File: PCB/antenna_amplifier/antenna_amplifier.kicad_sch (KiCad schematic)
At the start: 31 parts, among them J1 ANT_IN, J2 SPDIF_COAX, J3 PWR_IN, J4 ANT_BIAS, J5 AES_EBU, U1 LMP7721, U2 LMP7715, U3 PCM1808, U4 CS8406, U5 ADM7150-5.0, U6 ADM7150-3.3, U7 LMP7715, Y1 24.576MHz

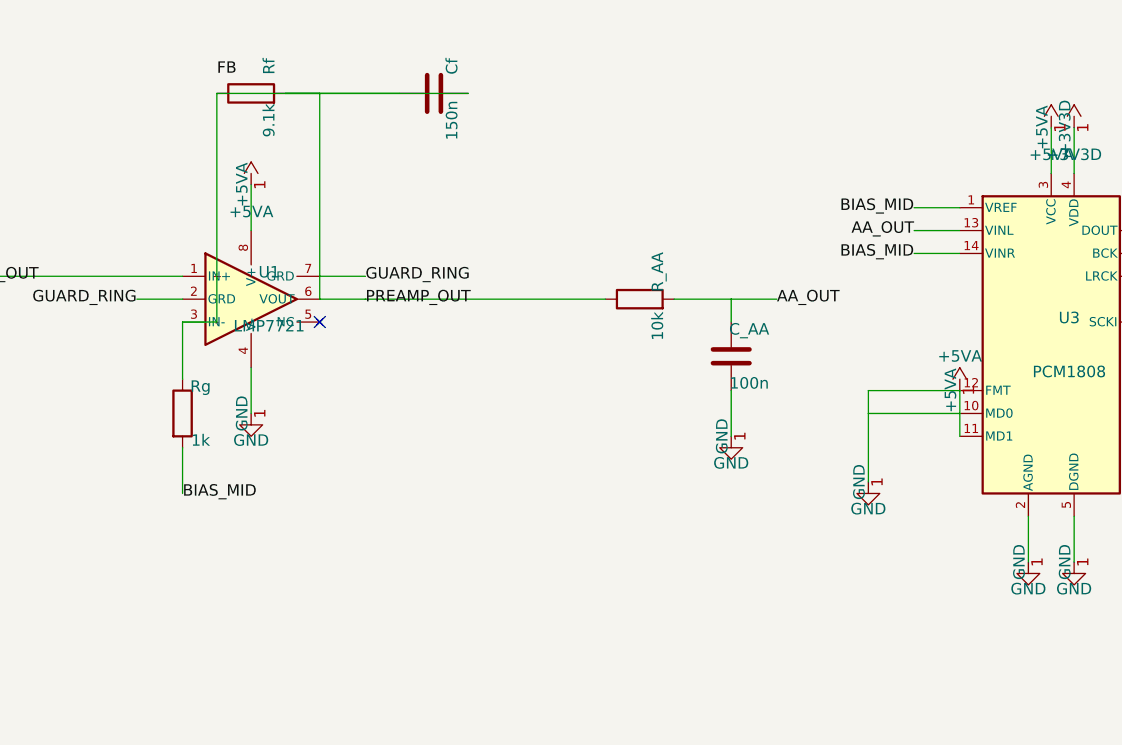
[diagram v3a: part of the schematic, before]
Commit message: Add DC coupling caps for 0dB DC gain and signal fidelity
Add Cg (100uF polypropylene) in series with Rg: blocks DC
through feedback divider so DC gain = 0 dB (unity). AC gain
remains 20 dB across ELF band. f_low = 1/(2pi*1k*100u) = 1.59 Hz
— gain is within 0.1 dB of 20 dB at SR1 (7.83 Hz).

Add C_out (10uF film) at LMP7721 output: blocks 2.5V DC bias
from reaching the PCM1808 ADC input. Combined with R_AA forms
a high-pass at 1.59 Hz — negligible loss at Schumann frequencies.

Add R_bias (47k) from PCM1808 VREF to VINL: sets ADC input
DC operating point to VREF/2 after the coupling cap, matching
the PCM1808 typical application circuit.

Gain profile:
  DC:           0 dB (blocked by Cg and C_out)
  1.6-117 Hz:  20 dB (flat across Schumann band)
  Above 117 Hz: rolls off -20dB/dec (via Cf)

Co-Authored-By: Claude Opus 4.6 (1M context) <noreply@anthropic.com>
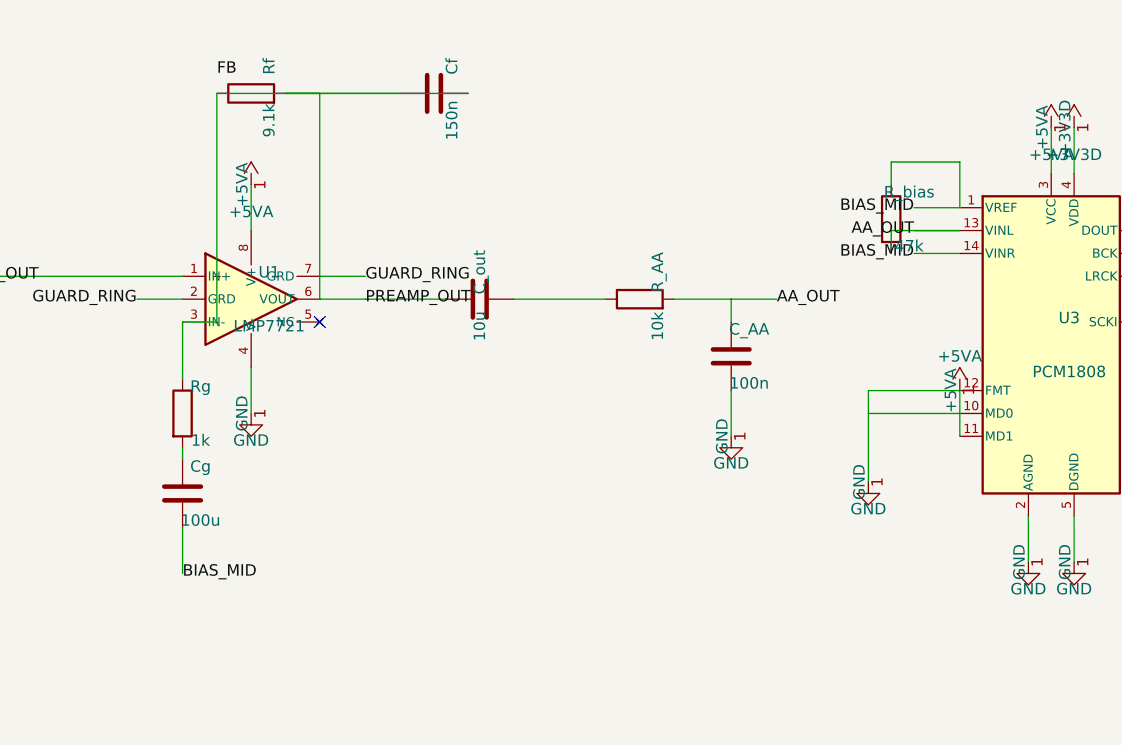
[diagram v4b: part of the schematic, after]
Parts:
- added C_out: 10u, symbol Device:C
- added Cg: 100u, symbol Device:C
- added R_bias: 47k, symbol Device:R
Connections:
- net AA_OUT: now also R_bias.2
- net BIAS_MID: now also Cg.2, R_bias.1; no longer Rg.2
- net PREAMP_OUT: now also C_out.1; no longer R_AA.1
- new net: Cg.1, Rg.2
- new net: C_out.2, R_AA.1
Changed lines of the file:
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@@
+		)
+	)
+	(symbol
+		(lib_id "Device:C")
+		(at 132.08 100.33 0)
+		(unit 1)
+		(exclude_from_sim no) (in_bom yes) (on_board yes) (dnp no)
+		(property "Reference" "Cg" (at 134.08 97.33 0) (effects (font (size 1.27 1.27))))
+		(property "Value" "100u" (at 134.08 103.33 0) (effects (font (size 1.27 1.27))))
+		(property "Datasheet" "~" (at 132.08 100.33 0) (effects (font (size 1.27 1.27)) (hide yes)))
+		(instances (project "antenna_amplifier"
+			(path "/09f45598-3e76-49a4-ba12-a3a92a2874f1" (reference "Cg") (unit 1)))))
+	(wire
+		(pts
+			(xy 132.08 95.25) (xy 132.08 96.52)
+		)
+		(stroke
+			(width 0)
+			(type solid)
 		)
 	)
 	(wire
 		(pts
-			(xy 132.08 95.25) (xy 132.08 100.33)
+			(xy 132.08 104.14) (xy 132.08 109.22)
 		)
 		(stroke
@@
 	)
 	(label "BIAS_MID"
-		(at 132.08 100.33 0)
+		(at 132.08 109.22 0)
 		(effects
 			(font
@@
 		(instances (project "antenna_amplifier"
 			(path "/09f45598-3e76-49a4-ba12-a3a92a2874f1" (reference "C_AA") (unit 1)))))
-	(wire (pts (xy 152.4 78.74) (xy 179.07 78.74))
+	(symbol
+		(lib_id "Device:C")
+		(at 165.1 78.74 90)
+		(unit 1)
+		(exclude_from_sim no) (in_bom yes) (on_board yes) (dnp no)
+		(property "Reference" "C_out" (at 165.1 75.74 0) (effects (font (size 1.27 1.27))))
+		(property "Value" "10u" (at 165.1 81.74 0) (effects (font (size 1.27 1.27))))
+		(property "Datasheet" "~" (at 165.1 78.74 0) (effects (font (size 1.27 1.27)) (hide yes)))
+		(instances (project "antenna_amplifier"
+			(path "/09f45598-3e76-49a4-ba12-a3a92a2874f1" (reference "C_out") (unit 1)))))
+	(wire (pts (xy 152.4 78.74) (xy 161.29 78.74))
+		(stroke (width 0) (type solid)))
+	(wire (pts (xy 168.91 78.74) (xy 179.07 78.74))
 		(stroke (width 0) (type solid)))
 	(wire (pts (xy 186.69 78.74) (xy 193.04 78.74))
@@
 		(instances (project "antenna_amplifier"
 			(path "/09f45598-3e76-49a4-ba12-a3a92a2874f1" (reference "#PWR70") (unit 1)))))
+	(symbol
+		(lib_id "Device:R")
+		(at 210.82 69.85 0)
+		(unit 1)
+		(exclude_from_sim no) (in_bom yes) (on_board yes) (dnp no)
+		(property "Reference" "R_bias" (at 212.82 66.85 0) (effects (font (size 1.27 1.27))))
+		(property "Value" "47k" (at 212.82 72.85 0) (effects (font (size 1.27 1.27))))
+		(property "Datasheet" "~" (at 210.82 69.85 0) (effects (font (size 1.27 1.27)) (hide yes)))
+		(instances (project "antenna_amplifier"
+			(path "/09f45598-3e76-49a4-ba12-a3a92a2874f1" (reference "R_bias") (unit 1)))))
+	(wire (pts (xy 210.82 66.04) (xy 210.82 63.5))
+		(stroke (width 0) (type solid)))
+	(wire (pts (xy 210.82 63.5) (xy 218.44 63.5))
+		(stroke (width 0) (type solid)))
+	(wire (pts (xy 218.44 63.5) (xy 218.44 68.58))
+		(stroke (width 0) (type solid)))
+	(wire (pts (xy 210.82 73.66) (xy 210.82 71.12))
+		(stroke (width 0) (type solid)))
+	(wire (pts (xy 210.82 71.12) (xy 218.44 71.12))
+		(stroke (width 0) (type solid)))
 	(no_connect
 		(at 147.32 81.28)

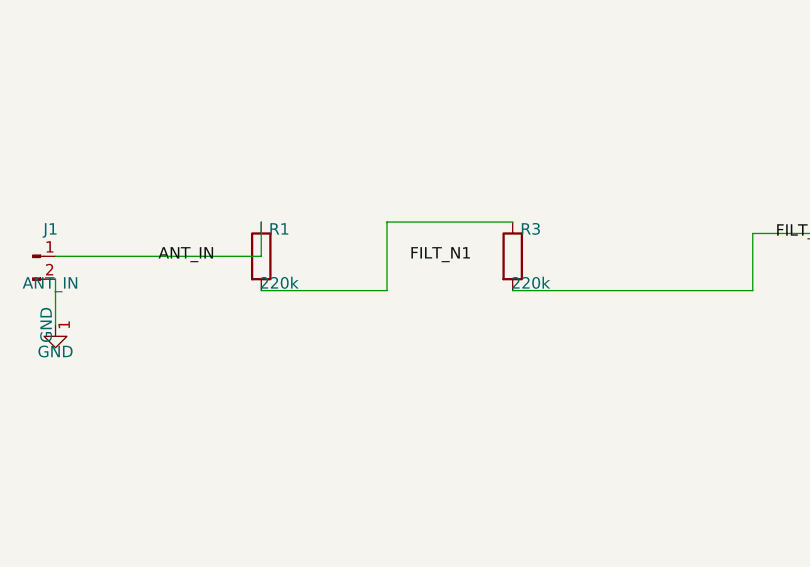
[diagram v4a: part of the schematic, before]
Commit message: Optimise input filter: R=33k, C=50pF for 2.3x noise reduction
Change filter resistors from 220k to 33k and caps from 45pF to
50pF (100pF total). This dramatically reduces the dominant noise
source (filter R thermal noise) while maintaining adequate RF
rejection:

  - Noise at antenna: 64.6 nV/rtHz (was 149.6 -> 2.3x better)
  - 3.2x better than Romero AD820 at SR1
  - FM rejection: -121 dB (was -154, still massive)
  - AM rejection: -41 dB (adequate for 15km AM tower)
  - Cap divider: -4.7 dB (was -4.3, acceptable)

Key insight: the RF filter doesn't need a low cutoff (96.5 kHz
is fine) because ELF band shaping is done by the preamp feedback
(117 Hz) and AA filter (159 Hz). The filter's only job is to
kill AM/FM before the LMP7721.

Updated: PLAN.md, schematic R1/R3 values, all 7 simulation
scripts and SVG plots.

Co-Authored-By: Claude Opus 4.6 (1M context) <noreply@anthropic.com>
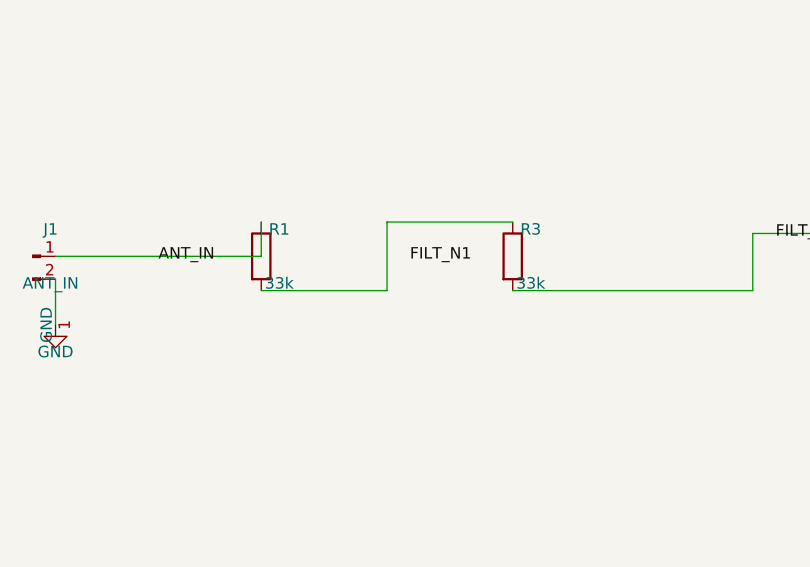
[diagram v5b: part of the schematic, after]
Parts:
- R1, R3: value 220k -> 33k
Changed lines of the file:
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@@
 			)
 		)
-		(property "Value" "220k"
+		(property "Value" "33k"
 			(at 52.8 81.74 0)
 			(effects
@@
 			)
 		)
-		(property "Value" "220k"
+		(property "Value" "33k"
 			(at 80.74 81.74 0)
 			(effects

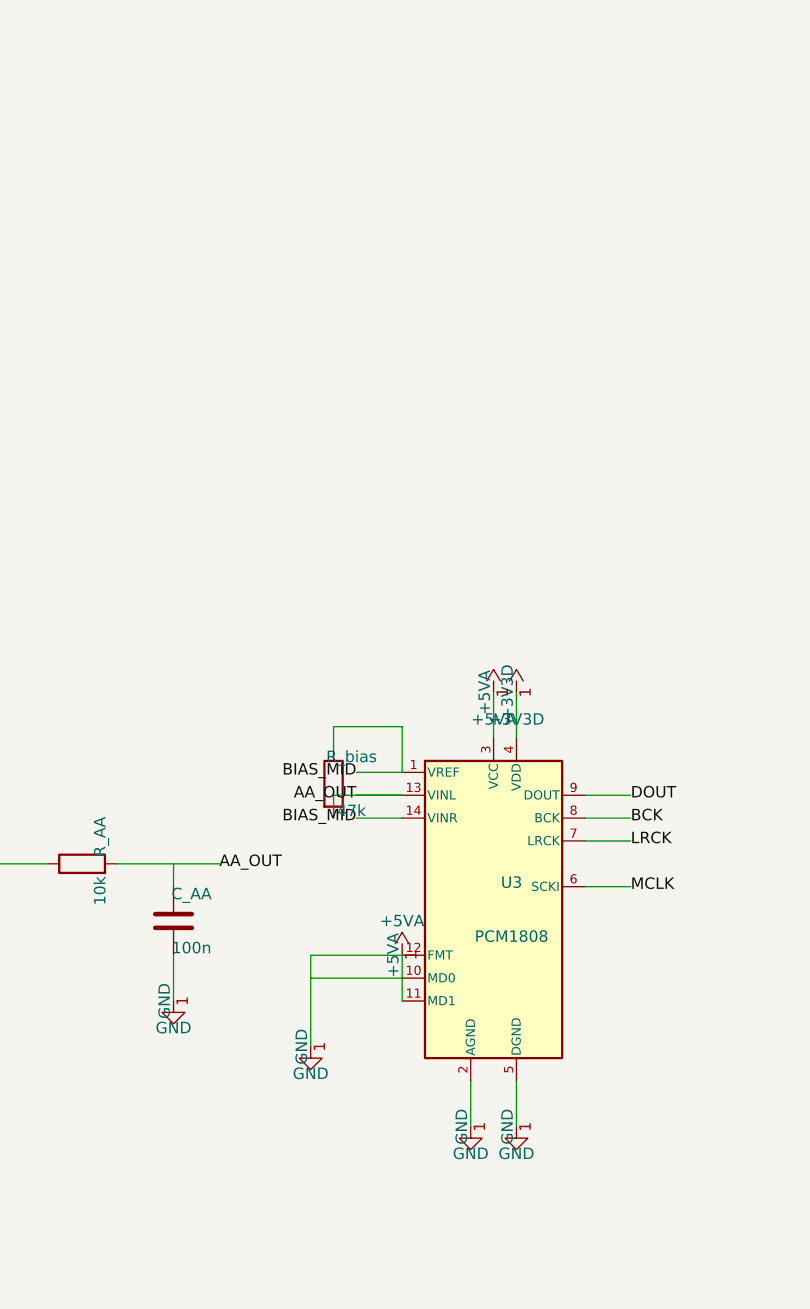
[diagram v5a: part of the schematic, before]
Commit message: Upgrade ADC from PCM1808 to PCM1804 (192kHz, 112dB DR)
Replace PCM1808 (96kHz, 99dB SNR, 14-pin TSSOP) with PCM1804
(192kHz, 112dB DR, 28-pin SSOP) for maximum SPDIF fidelity.

ADC noise floor drops from 54.3 to 16.1 nV/rtHz (3.4x better).
The ADC is now transparent — its noise is below the preamp's
input-referred noise. System is entirely analog-limited.

Key specs: 5V analog + 3.3V digital (same rails), differential
input (VINL- tied to VCOML for single-ended), I2S output,
128/256/384/512/768 fs clock ratios.

For 192kHz: OSR2=H, OSR1=H, OSR0=H (quad rate, 128xfs).
Existing 24.576 MHz oscillator works perfectly.

New PCM1804 symbol added to project library (28-pin SSOP).
Schematic wiring partially updated — needs completion in
KiCad GUI for the new 28-pin layout.

Updated simulation: feedback_tradeoff.py now models PCM1804
(5Vpp full-scale, 111dB SNR, 192kHz).

Co-Authored-By: Claude Opus 4.6 (1M context) <noreply@anthropic.com>
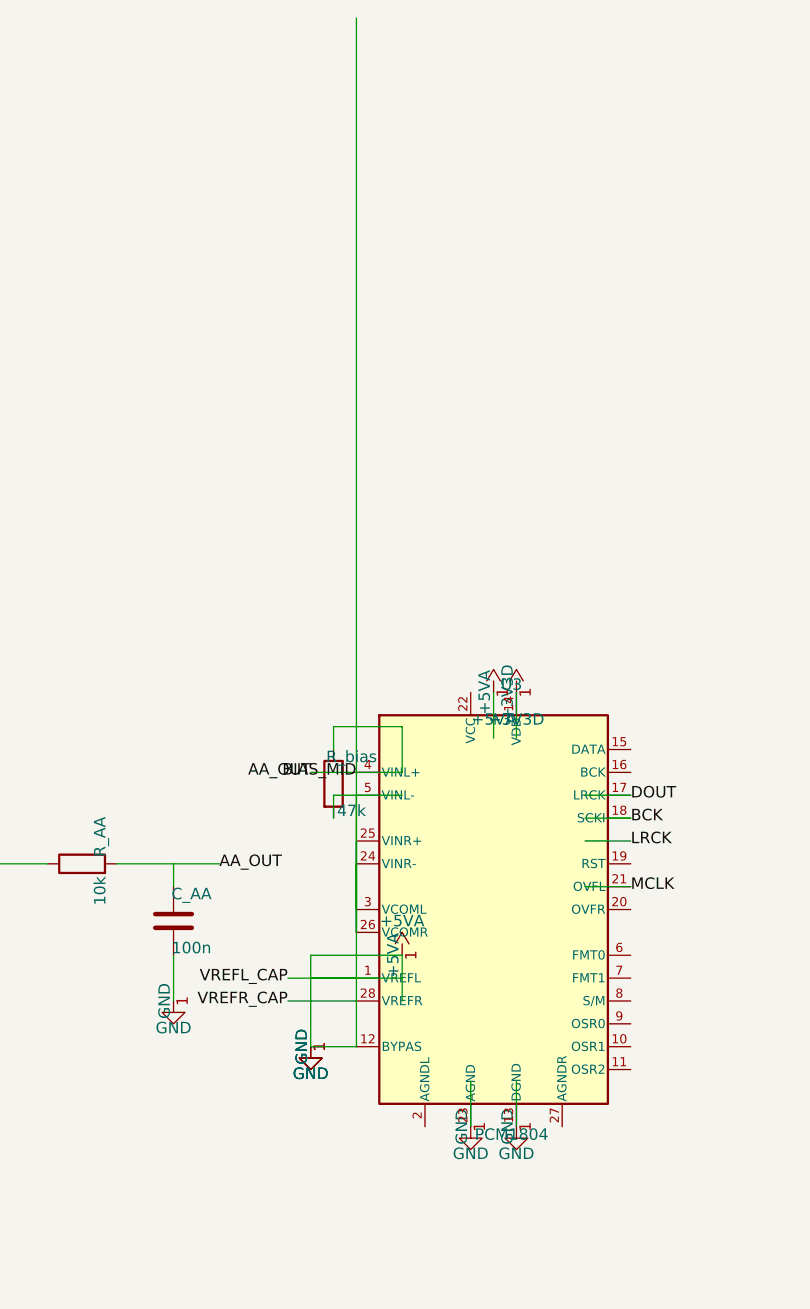
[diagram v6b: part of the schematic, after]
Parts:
- U3: value PCM1808 -> PCM1804; footprint Package_SO:TSSOP-14_4.4x5mm_P0.65mm -> Package_SO:SSOP-28_5.3x10.2mm_P0.65mm; symbol antenna_amplifier:PCM1808 -> antenna_amplifier:PCM1804
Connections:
- net +3V3D: now also U3.14 (VDD); no longer U3.4 (VDD)
- net +5VA: now also C7.1, C_AA.1, Cg.2, R5.2, R6.1, R_AA.2, R_bias.1, U3.1 (VREFL), U3.13 (DGND), U3.23 (AGND), U3.24 (VINR-), U3.25 (VINR+), U3.26 (VCOMR), U3.4 (VINL+), U7.3 (+IN); no longer U3.10 (MD0), U3.11 (MD1), U3.2 (AGND)
- net BCK: now also U3.18 (SCKI); no longer U3.8 (BCK)
- net DOUT: now also U3.17 (LRCK); no longer U3.9 (DOUT)
- net LRCK: no longer U3.7 (LRCK)
- net MCLK: now also U3.21 (OVFL); no longer U3.6 (SCKI)
- removed net AA_OUT: C_AA.1, R_AA.2, R_bias.2, U3.13 (VINL)
- removed net BIAS_MID: C7.1, Cg.2, R5.2, R6.1, R_bias.1, U3.1 (VREF), U3.14 (VINR), U7.3 (+IN)
- new net VREFR_CAP: U3.28 (VREFR)
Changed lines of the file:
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@@
 	)
 	(symbol
-		(lib_id "antenna_amplifier:PCM1808")
+		(lib_id "antenna_amplifier:PCM1804")
 		(at 228.6 83.82 0)
 		(unit 1)
-		(exclude_from_sim no)
-		(in_bom yes)
-		(on_board yes)
-		(dnp no)
-		(property "Reference" "U3"
-			(at 230.6 80.82 0)
-			(effects
-				(font
-					(size 1.27 1.27)
-				)
-			)
-		)
-		(property "Value" "PCM1808"
-			(at 230.6 86.82 0)
-			(effects
-				(font
-					(size 1.27 1.27)
-				)
-			)
-		)
-		(property "Footprint" "Package_SO:TSSOP-14_4.4x5mm_P0.65mm"
-			(at 228.6 83.82 0)
-			(effects
-				(font
-					(size 1.27 1.27)
-				)
-				(hide yes)
-			)
-		)
-		(property "Datasheet" "~"
-			(at 228.6 83.82 0)
-			(effects
-				(font
-					(size 1.27 1.27)
-				)
-				(hide yes)
-			)
-		)
-		(instances
-			(project "antenna_amplifier"
-				(path "/09f45598-3e76-49a4-ba12-a3a92a2874f1"
-					(reference "U3")
-					(unit 1)
-				)
-			)
-		)
+		(exclude_from_sim no) (in_bom yes) (on_board yes) (dnp no)
+		(property "Reference" "U3" (at 230.6 58.82 0)
+			(effects (font (size 1.27 1.27))))
+		(property "Value" "PCM1804" (at 230.6 108.82 0)
+			(effects (font (size 1.27 1.27))))
+		(property "Footprint" "Package_SO:SSOP-28_5.3x10.2mm_P0.65mm" (at 228.6 83.82 0)
+			(effects (font (size 1.27 1.27)) (hide yes)))
+		(property "Datasheet" "https://www.ti.com/lit/ds/symlink/pcm1804.pdf" (at 228.6 83.82 0)
+			(effects (font (size 1.27 1.27)) (hide yes)))
+		(instances (project "antenna_amplifier"
+			(path "/09f45598-3e76-49a4-ba12-a3a92a2874f1" (reference "U3") (unit 1))))
 	)
 	(symbol
@@
 		)
 	)
-	(wire
-		(pts
-			(xy 218.44 71.12) (xy 213.36 71.12)
-		)
-		(stroke
-			(width 0)
-			(type solid)
-		)
-	)
-	(label "AA_OUT"
-		(at 213.36 71.12 180)
-		(effects
-			(font
-				(size 1.27 1.27)
-			)
-		)
-	)
-	(wire
-		(pts
-			(xy 218.44 73.66) (xy 213.36 73.66)
-		)
-		(stroke
-			(width 0)
-			(type solid)
-		)
-	)
-	(label "BIAS_MID"
-		(at 213.36 73.66 180)
-		(effects
-			(font
-				(size 1.27 1.27)
-			)
-		)
-	)
-	(wire
-		(pts
+	(wire (pts (xy 213.36 68.58) (xy 208.28 68.58))
+		(stroke (width 0) (type solid)))
+	(label "AA_OUT" (at 208.28 68.58 180)
+		(effects (font (size 1.27 1.27))))
+	(wire (pts (xy 213.36 71.12) (xy 213.36 83.82))
+		(stroke (width 0) (type solid)))
+	(wire (pts (xy 213.36 76.2) (xy 213.36 86.36))
+		(stroke (width 0) (type solid)))
+	(wire (pts (xy 213.36 78.74) (xy 213.36 86.36))
+		(stroke (width 0) (type solid)))
+	(wire (pts (xy 213.36 -15.24) (xy 213.36 99.06))
+		(stroke (width 0) (type solid)))
+	(wire (pts (xy 213.36 99.06) (xy 208.28 99.06))
+		(stroke (width 0) (type solid)))
+	(symbol
+		(lib_id "power:GND")
+		(at 208.28 99.06 0)
+		(unit 1)
+		(exclude_from_sim no) (in_bom yes) (on_board yes) (dnp no)
+		(property "Reference" "#PWR90" (at 208.28 97.06 0) (effects (font (size 1.27 1.27)) (hide yes)))
+		(property "Value" "GND" (at 208.28 102.06 0) (effects (font (size 1.27 1.27))))
+		(instances (project "antenna_amplifier"
+			(path "/09f45598-3e76-49a4-ba12-a3a92a2874f1" (reference "#PWR90") (unit 1)))))
+	(wire (pts (xy 213.36 91.44) (xy 205.74 91.44))
+		(stroke (width 0) (type solid)))
+	(label "VREFL_CAP" (at 205.74 91.44 180)
+		(effects (font (size 1.27 1.27))))
+	(wire (pts (xy 213.36 93.98) (xy 205.74 93.98))
+		(stroke (width 0) (type solid)))
+	(label "VREFR_CAP" (at 205.74 93.98 180)
+		(effects (font (size 1.27 1.27))))
+	(wire
+		(pts
